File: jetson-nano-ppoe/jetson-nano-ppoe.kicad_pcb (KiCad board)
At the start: 2 copper layers, 14 x 79 mm, 33 parts, among them IC1 TPS566238PRQFR, J1 Conn_01x02, J2 Conn_02x05_Odd_Even, J3 Conn_02x02_Odd_Even, Q1 Q_PMOS_GSD, Q2 Q_PMOS_GSD, Q4 Q_NMOS_DUAL

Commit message: update jetson-nano-ppoe for pololu reg
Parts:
- removed C1, C2: 22uF 25V, Capacitors_SMD:C_0805
- removed C10, C11, C8, C9: 22uF, Capacitors_SMD:C_0805
- removed C12: 0.1uF, Capacitors_SMD:C_0603
- removed C3, C6: 0.1uF 25V, Capacitors_SMD:C_0603
- removed C4: 1uF, Capacitors_SMD:C_0603
- removed C5: 10nF, Capacitors_SMD:C_0603
- removed C7: 33pF, Capacitors_SMD:C_0603
- removed D4: 5.1V, Diode_SMD:D_SOD-323_HandSoldering
- removed IC1: TPS566238PRQFR, SamacSys_Parts:TPS566238PRQFR
- removed L1: 2.2uH 13.2mOhm, Inductors_SMD:L_Coilcraft_XAL5030
- removed Q1: Q_PMOS_GSD, Package_TO_SOT_SMD:SOT-23
- removed R3: 0, Resistors_SMD:R_0603
- removed R4: 220k, Resistors_SMD:R_0603
- removed R5: 30k, Resistors_SMD:R_0603
- added J4: Conn_02x06_Odd_Even, Connector_PinHeader_2.54mm:PinHeader_2x06_P2.54mm_Vertical, F.Cu at (148.7, 78.8)
- added J5: Conn_01x06, Connector_PinHeader_2.54mm:PinHeader_1x06_P2.54mm_Vertical, F.Cu at (157.6, 120.7)
- added JP1: SolderJumper_2_Open, Jumper:SolderJumper-2_P1.3mm_Open_TrianglePad1.0x1.5mm, B.Cu at (154.5, 118.0)
- added NT1: NetTie_2, NetTie:NetTie-2_SMD_Pad2.0mm, F.Cu at (151.5, 129.5)
- added NT2: NetTie_2, NetTie:NetTie-2_SMD_Pad2.0mm, F.Cu at (148.8, 93.5)
- D3: value 5.1V -> Green; footprint Diode_SMD:D_SOD-323_HandSoldering -> LED_SMD:LED_0603_1608Metric
- moved RN1 31.0 mm to (157.0, 92.8)
- moved D3 14.3 mm to (157.8, 99.2), turned to 180 degrees
- moved G*** 10.7 mm to (153.8, 98.0)
- moved Q4 9.42 mm to (157.0, 86.8)
- moved RN2 9.42 mm to (157.0, 81.0)
- moved Q2 5.34 mm to (154.0, 72.2)
- moved D1 0.47 mm to (157.9, 131.2), turned to 180 degrees
- moved D2 0.47 mm to (157.8, 71.4), turned to 0 degrees
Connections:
- net /12V_CONN_K renamed /REG_VIN_K
- D2 pad 1: /TR2_TAP_K -> /REG_VRP_K
- D2 pad 2: +12V -> /REG_VRP
- D3 pad 1: +12V -> /REG_PG_R
- D3 pad 2: /12V_G -> +12V
- J2 pad 7: Net-(J2-Pad7) -> unconnected-(J2-Pad7)
- Q2 pad 2: +12V -> /REG_VRP
- Q4 pad 2: /12V_CONN_R -> +12V
- Q4 pad 3: /12V_2_G_R -> +12V
- Q4 pad 5: /TR2_TAP_R -> /TR2_TAP
- RN1 pad 1: /12V_CONN -> unconnected-(RN1-Pad1)
- RN1 pad 4: /12V_G_R -> /REG_PG
- RN1 pad 5: /12V_G -> /REG_PG_R
- RN1 pad 7: /12V_CONN_R -> +12V
- RN1 pad 8: /12V_CONN_R -> unconnected-(RN1-Pad8)
- RN2 pad 2: GND -> /12V_2_G
- RN2 pad 3: /12V_2_G_R -> /12V_2_G
- RN2 pad 4: /12V_2_G_R -> /REG_VRP_K
- RN2 pad 5: /12V_2_G -> +12V
- RN2 pad 6: /TR2_TAP_K -> /REG_VRP
- RN2 pad 7: /TR2_TAP_R -> +12V
- RN2 pad 8: /TR2_TAP_R -> GND
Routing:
- net /12V_G_R: track 86.0 -> 7.24 mm, vias 2 -> 0
- net /12V_CONN_R: track 48.0 -> 0.00 mm, vias 2 -> 0
- net /REG_VRP: track 0.00 -> 30.9 mm, vias 0 -> 2
- net /REG_VIN_K: track 9.32 -> 38.6 mm
- net /REG_PG: track 0.00 -> 25.8 mm, vias 0 -> 2
- net GND: track 30.3 -> 8.06 mm, vias 24 -> 4
- net /12V_CONN: track 17.9 -> 0.00 mm
- net /TR2_TAP: track 15.4 -> 31.6 mm, vias 0 -> 2
- net +12V: track 11.9 -> 25.8 mm
- net /12V_G: track 13.7 -> 0.00 mm
- net /IC1_FB: track 13.6 -> 0.00 mm, vias 2 -> 0
- net +5V: track 24.3 -> 11.4 mm
- net /REG_VRP_K: track 0.00 -> 12.8 mm
- net /UART1_RXD: track 0.00 -> 12.3 mm, vias 0 -> 1
- net /TR2_TAP_R: track 10.7 -> 0.00 mm, vias 2 -> 0
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- removed copper zone on F.Cu, net /IC1_SW
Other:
- net class Default removed
- board text added: "<"
- board text added: ">"
- board text added: "EN"
- board text added: "GND"
- board text added: "PG"
- board text added: "REG PG"
- board text added: "RXD"
- board text added: "TXD"
- board text added: "UART"
- board text added: "VO"

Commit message: add gigablox-nano-rvp and simplify jetson-nano-ppoe
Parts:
- removed D1: Green, LED_SMD:LED_0603_1608Metric
- removed Q4: Q_NMOS_DUAL, Package_TO_SOT_SMD:SOT-23-6
- removed RN1: 10k, Resistor_SMD:R_Array_Convex_4x1206
- added R1: 15k, Resistor_SMD:R_0805_2012Metric, F.Cu at (166.8, 82.5)
- RN2: value 10k -> 15k
- moved D3 29.1 mm to (149.0, 71.5), turned to 0 degrees
- moved G*** 0.75 mm to (154.5, 98.0)
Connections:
- net /12V_2_G renamed /TR2_EN
- D2 pad 2: /REG_VRP -> +12V
- J4 pad 3: /REG_VRP -> +12V
- J4 pad 4: /REG_VRP -> +12V
- J4 pad 5: +12V -> /REG_VIN
- J4 pad 6: +12V -> /REG_VIN
- NT1 pad 2: +12V -> /REG_VIN
- Q2 pad 2: /REG_VRP -> +12V
- RN2 pad 1: /TR2_TAP -> /REG_PG_R
- RN2 pad 5: +12V -> GND
- RN2 pad 6: /REG_VRP -> +12V
- RN2 pad 7: +12V -> /REG_VIN
- RN2 pad 8: GND -> /REG_PG
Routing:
- net /REG_VIN_K: track 38.6 -> 0.00 mm
- net /REG_VRP: track 30.9 -> 0.00 mm, vias 2 -> 0
- net /TR2_TAP: track 31.6 -> 11.6 mm, vias 2 -> 0
- net /REG_PG_R: track 4.77 -> 13.2 mm, vias 0 -> 2
- net (no net): track 0.00 -> 8.29 mm
- net /12V_G_R: track 7.24 -> 0.00 mm
- net GND: track 8.06 -> 13.8 mm, vias 4 -> 1
- net +12V: track 25.8 -> 31.2 mm, vias 0 -> 2
- net /REG_VIN: track 0.00 -> 5.40 mm
- added copper zone on F.Cu, net /REG_VIN
- removed copper zone on F.Cu, net +12V
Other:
- board text added: "PWR IN"
- board text removed: "PPOE PWR"
- board text removed: "REG PG"

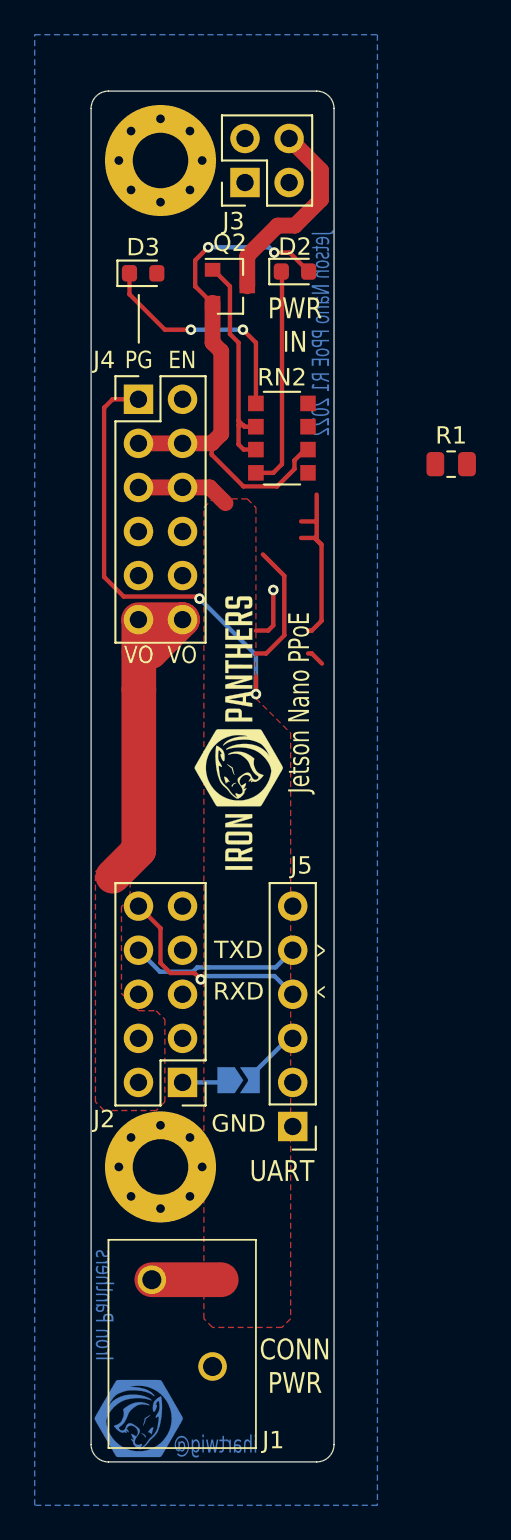
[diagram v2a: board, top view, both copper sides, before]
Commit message: new jetson-nano-ppoe and gigablox-nano-rvp gerbers
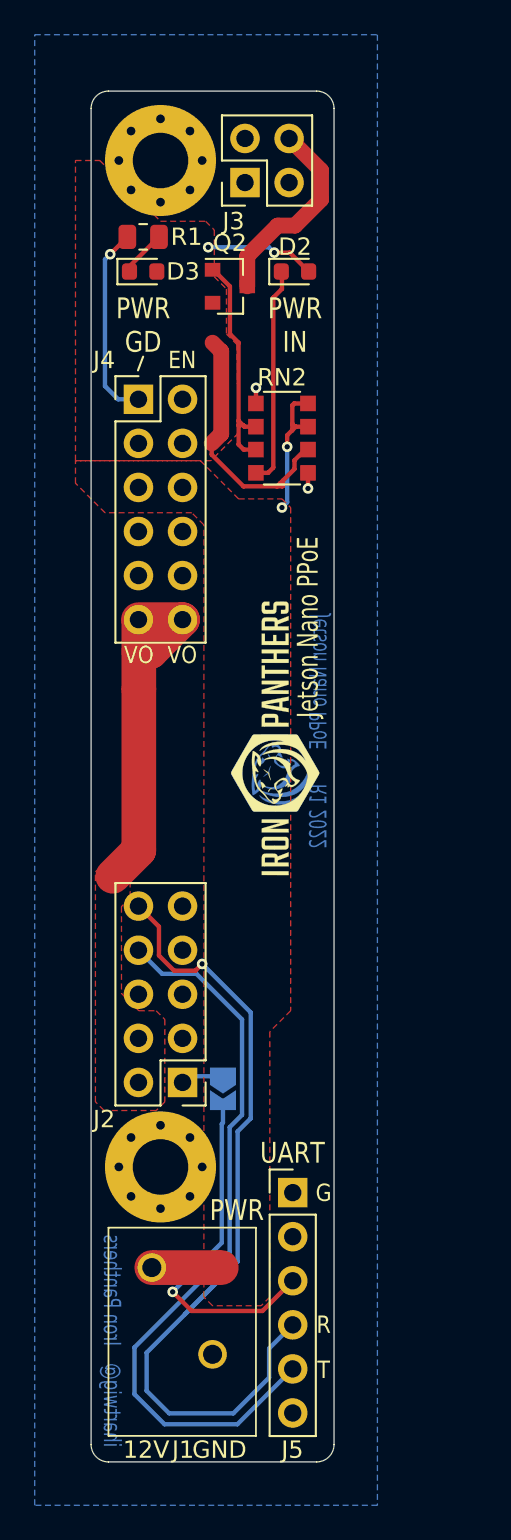
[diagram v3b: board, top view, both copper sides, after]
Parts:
- moved G*** 38.0 mm to (156.6, 100.3), turned to -90 degrees
- moved R1 22.1 mm to (149.0, 69.4), turned to 180 degrees
- moved J5 3.81 mm to (157.6, 124.5), turned to 0 degrees
- moved G*** 2.12 mm to (156.6, 98.3)
- moved JP1 1.03 mm to (153.6, 118.5), turned to -90 degrees
- moved J1 0.70 mm to (153.0, 133.8)
- moved NT1 0.70 mm to (151.5, 128.8)
- moved D3 0.10 mm to (149.0, 71.4)
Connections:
- R1 pad 1: /REG_VIN -> /REG_PG_R
- R1 pad 2: GND -> /REG_PG
- RN2 pad 1: /REG_PG_R -> GND
- RN2 pad 8: /REG_PG -> /REG_VIN
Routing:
- net /UART1_RXD: track 12.3 -> 50.5 mm
- net /UART1_TXD: track 9.92 -> 42.9 mm
- net /UART_VCC: track 3.48 -> 20.3 mm, vias 0 -> 1
- net /REG_PG: track 25.8 -> 11.4 mm, vias 2 -> 1
- net GND: track 13.8 -> 1.80 mm, vias 1 -> 2
- net /REG_PG_R: track 13.2 -> 2.70 mm, vias 2 -> 0
- net +12V: track 31.2 -> 21.6 mm
- net (no net): track 8.29 -> 0.00 mm
- net /REG_VIN: track 5.40 -> 8.37 mm, vias 0 -> 2
- added copper zone on F.Cu, net +12V
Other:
- board text added: "12V GND"
- board text added: "3V3 on UART"
- board text added: "G"
- board text added: "PWR"
- board text added: "PWR GD"
- board text added: "R"
- board text added: "T"
- board text removed: "<"
- board text removed: ">"
- board text removed: "CONN PWR"
- board text removed: "GND"
- board text removed: "PG"
- board text removed: "RXD"
- board text removed: "TXD"

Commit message: gigablox-nano-rvp and jetson-nano-ppoe gerbers
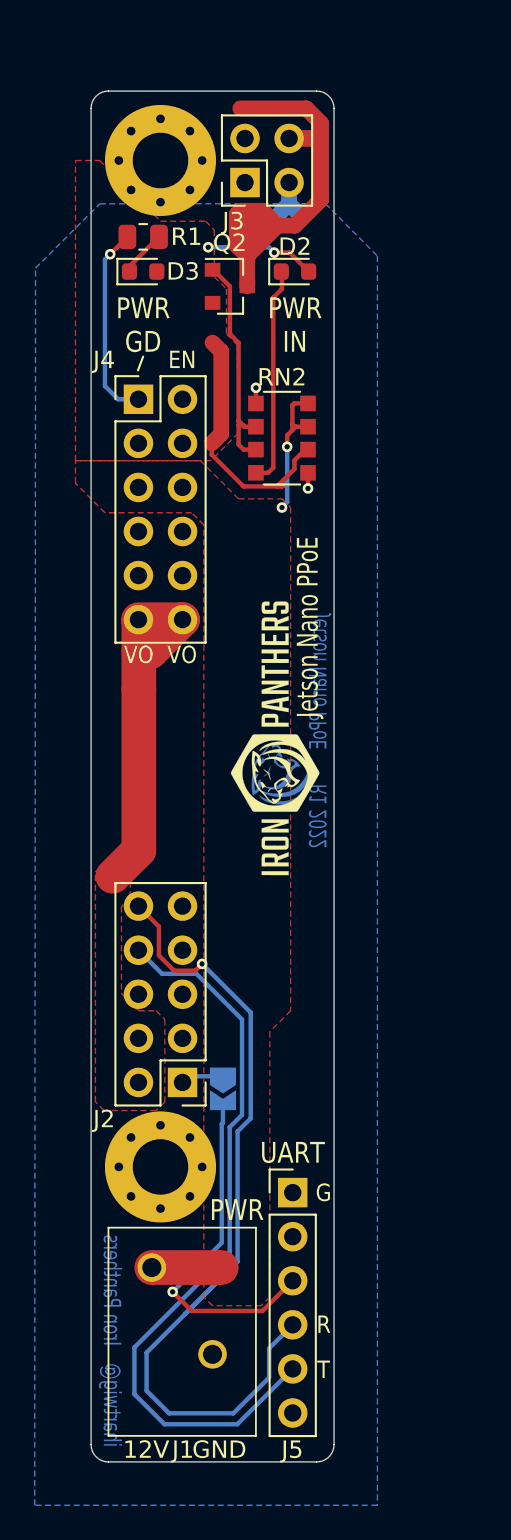
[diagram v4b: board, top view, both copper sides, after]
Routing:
- net /TR2_TAP: track 11.6 -> 29.2 mm
- net GND: track 1.80 -> 4.30 mm
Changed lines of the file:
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@@
     (property "Sheetname" "")
     (attr through_hole)
-    (fp_text reference "J3" (at -2.23 -0.665 180) (layer "F.SilkS")
+    (fp_text reference "J3" (at -2.23 -0.665) (layer "F.SilkS")
       (effects (font (size 1 1) (thickness 0.15)))
     )
@@
   (via (at 158.5 83.9) (size 0.6096) (drill 0.3048) (layers "F.Cu" "B.Cu") (net 2))
   (via (at 155.5 78.1) (size 0.6096) (drill 0.3048) (layers "F.Cu" "B.Cu") (net 2))
+  (segment (start 157.41 67.51) (end 157.8 67.9) (width 0.9144) (layer "B.Cu") (net 2))
+  (segment (start 157.41 66.27) (end 157.41 67.51) (width 0.9144) (layer "B.Cu") (net 2))
+  (segment (start 157.41 67.51) (end 157.39 67.51) (width 0.9144) (layer "B.Cu") (net 2))
+  (segment (start 157.39 67.51) (end 156.9 68) (width 0.9144) (layer "B.Cu") (net 2))
   (segment (start 148.75 104.75) (end 147.25 106.25) (width 2) (layer "F.Cu") (net 3))
   (segment (start 148.75 95.5) (end 148.75 104.75) (width 2) (layer "F.Cu") (net 3))
@@
   (segment (start 151.625 117.775) (end 151.27 118.13) (width 0.254) (layer "B.Cu") (net 8))
   (segment (start 153.6 117.775) (end 151.625 117.775) (width 0.254) (layer "B.Cu") (net 8))
+  (segment (start 154.4 69.9) (end 155 70.5) (width 0.9144) (layer "F.Cu") (net 12))
+  (segment (start 155.8 69.7) (end 155.8 68.8) (width 0.9144) (layer "F.Cu") (net 12))
+  (segment (start 156.75 68.75) (end 155.9 67.9) (width 0.9144) (layer "F.Cu") (net 12))
+  (segment (start 156.75 68.75) (end 155.8 69.7) (width 0.9144) (layer "F.Cu") (net 12))
+  (segment (start 155 70.5) (end 155 68.8) (width 0.9144) (layer "F.Cu") (net 12))
+  (segment (start 159.25 64.15) (end 159.25 67.25) (width 0.9144) (layer "F.Cu") (net 12))
+  (segment (start 155 70.5) (end 155.8 69.7) (width 0.9144) (layer "F.Cu") (net 12))
+  (segment (start 158.83 63.73) (end 159.25 64.15) (width 0.9144) (layer "F.Cu") (net 12))
+  (segment (start 155.9 67.9) (end 154.6 67.9) (width 0.9144) (layer "F.Cu") (net 12))
+  (segment (start 157.41 63.73) (end 158.83 63.73) (width 0.9144) (layer "F.Cu") (net 12))
+  (segment (start 159.25 63.35) (end 159.25 62.85) (width 0.9144) (layer "F.Cu") (net 12))
+  (segment (start 158.87 63.73) (end 159.25 63.35) (width 0.9144) (layer "F.Cu") (net 12))
+  (segment (start 157.41 63.73) (end 158.87 63.73) (width 0.9144) (layer "F.Cu") (net 12))
+  (segment (start 154.4 68.1) (end 154.4 69.9) (width 0.9144) (layer "F.Cu") (net 12))
+  (segment (start 155 70.5) (end 155 72.25) (width 0.9144) (layer "F.Cu") (net 12))
+  (segment (start 159.25 63.35) (end 159.25 64.15) (width 0.9144) (layer "F.Cu") (net 12))
   (segment (start 159.25 67.25) (end 157.75 68.75) (width 0.9144) (layer "F.Cu") (net 12))
-  (segment (start 159.25 65.57) (end 159.25 67.25) (width 0.9144) (layer "F.Cu") (net 12))
-  (segment (start 155 70.5) (end 156.75 68.75) (width 0.9144) (layer "F.Cu") (net 12))
+  (segment (start 158.4 62) (end 154.6 62) (width 0.9144) (layer "F.Cu") (net 12))
+  (segment (start 159.25 62.85) (end 158.4 62) (width 0.9144) (layer "F.Cu") (net 12))
+  (segment (start 155 68.8) (end 155.3 68.5) (width 0.9144) (layer "F.Cu") (net 12))
+  (segment (start 154.6 67.9) (end 154.4 68.1) (width 0.9144) (layer "F.Cu") (net 12))
   (segment (start 157.75 68.75) (end 156.75 68.75) (width 0.9144) (layer "F.Cu") (net 12))
-  (segment (start 155 72.25) (end 155 70.5) (width 0.9144) (layer "F.Cu") (net 12))
-  (segment (start 157.41 63.73) (end 159.25 65.57) (width 0.9144) (layer "F.Cu") (net 12))
   (segment (start 157 72.4) (end 157 71.4375) (width 0.254) (layer "F.Cu") (net 13))
   (segment (start 156.5 72.9) (end 157 72.4) (width 0.254) (layer "F.Cu") (net 13))
@@
         (xy 162.5 142.5)
         (xy 142.75 142.5)
-        (xy 142.75 57.75)
-        (xy 162.5 57.75)
+        (xy 142.8 71.2)
+        (xy 146.5 67.5)
+        (xy 159.500077 67.484811)
+        (xy 162.5 70.5)
       )
     )
@@
       )
     )
+  )
+  (zone (net 0) (net_name "") (layer "B.Mask") (hatch edge 0.508)
+    (connect_pads (clearance 0.3048))
+    (min_thickness 0.254) (filled_areas_thickness no)
+    (fill yes (thermal_gap 0.508) (thermal_bridge_width 0.508))
+    (polygon
+      (pts
+        (xy 155.7 68.8)
+        (xy 154.1 68.8)
+        (xy 154.1 67.6)
+        (xy 155.7 67.6)
+      )
+    )
+  )
+  (zone (net 0) (net_name "") (layer "F.Mask") (hatch edge 0.508)
+    (connect_pads (clearance 0.3048))
+    (min_thickness 0.254) (filled_areas_thickness no)
+    (fill yes (thermal_gap 0.508) (thermal_bridge_width 0.508))
+    (polygon
+      (pts
+        (xy 155.6 61.8)
+        (xy 155.6 62.2)
+        (xy 155.4 62.4)
+        (xy 154.4 62.4)
+        (xy 154.2 62.2)
+        (xy 154.2 61.8)
+        (xy 154.4 61.6)
+        (xy 155.4 61.6)
+      )
+    )
